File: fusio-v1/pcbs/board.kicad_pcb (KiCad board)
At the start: 2 copper layers, 210.5 x 76.5 mm, 72 parts

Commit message: add jlc silkscreen
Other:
- board text added: "JLCJLCJLCJLC"
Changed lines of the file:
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@@
 		(layer "Edge.Cuts")
+	)
+	(gr_text "JLCJLCJLCJLC"
+		(at 232.41 183.82 0)
+		(layer "B.SilkS")
+		(effects
+			(font
+				(size 1.5 1.5)
+				(thickness 0.3)
+				(bold yes)
+			)
+			(justify left bottom mirror)
+		)
 	)
 	(segment

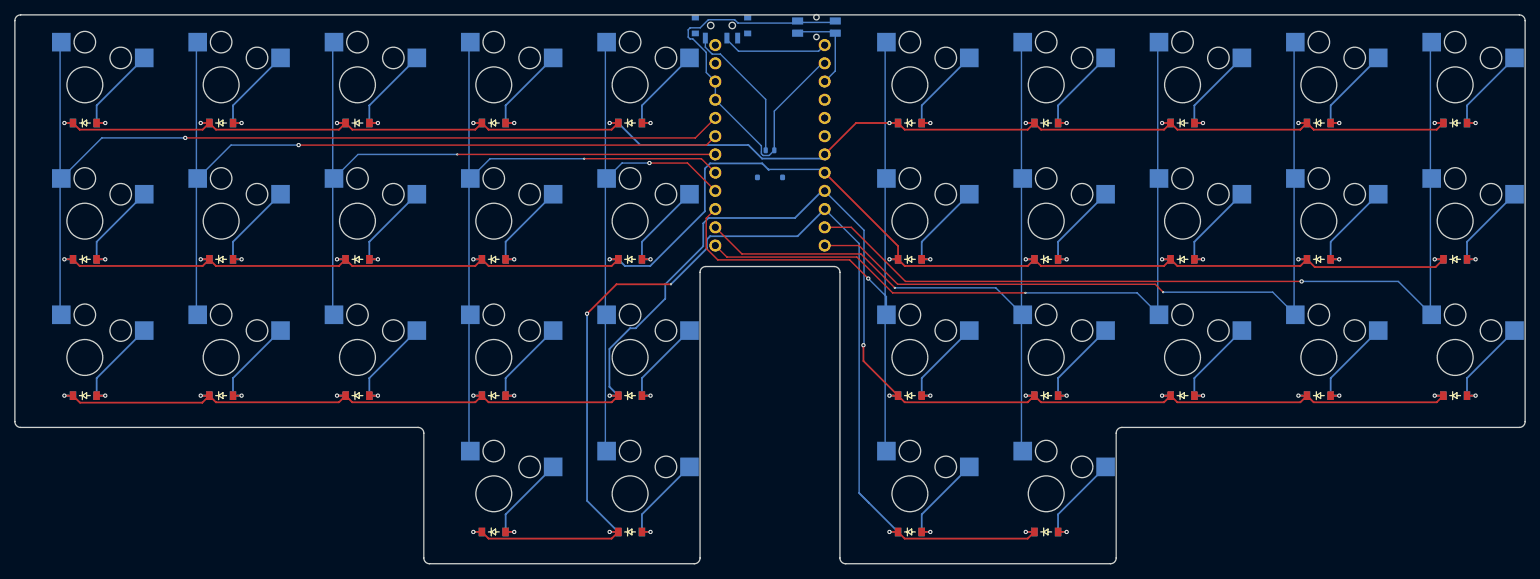
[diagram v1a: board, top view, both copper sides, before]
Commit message: support gateron
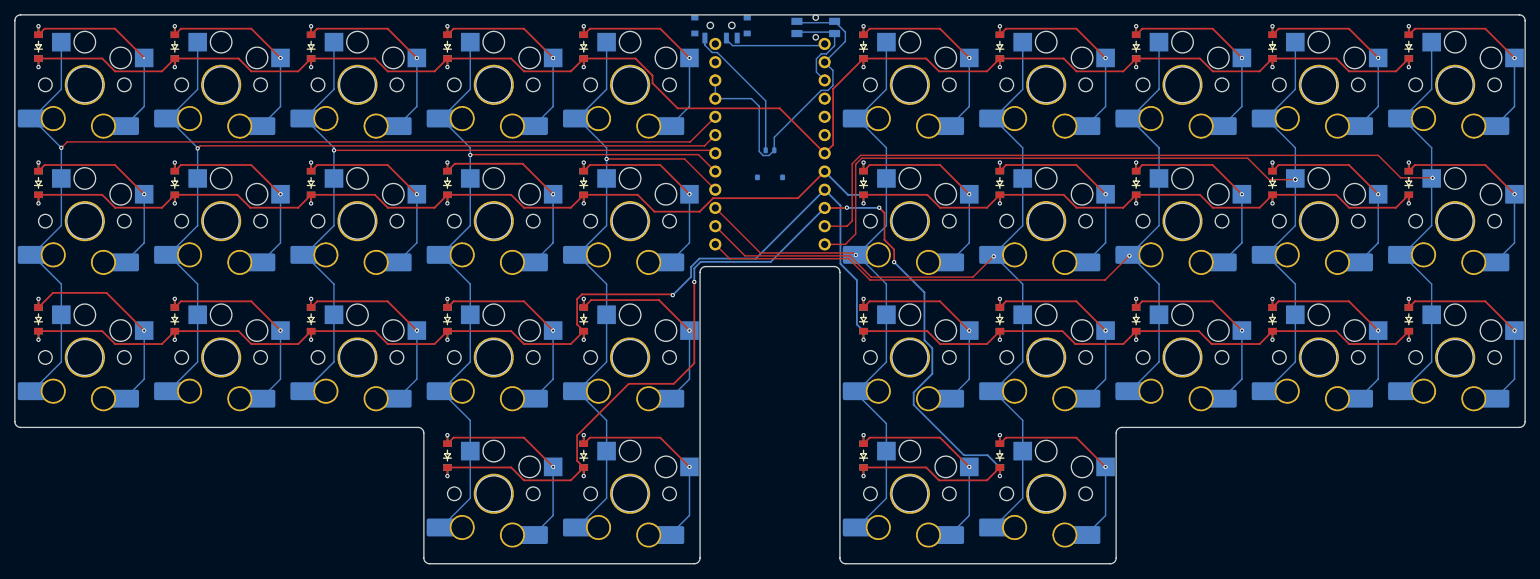
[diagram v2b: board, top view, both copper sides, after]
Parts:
- added S35: , ceoloide:switch_choc_v1_v2, B.Cu at (100.0, 156.0)
- added S36: , ceoloide:switch_choc_v1_v2, B.Cu at (100.0, 137.0)
- added S37: , ceoloide:switch_choc_v1_v2, B.Cu at (100.0, 118.0)
- added S38: , ceoloide:switch_choc_v1_v2, B.Cu at (119.0, 156.0)
- added S39: , ceoloide:switch_choc_v1_v2, B.Cu at (119.0, 137.0)
- added S40: , ceoloide:switch_choc_v1_v2, B.Cu at (119.0, 118.0)
- added S41: , ceoloide:switch_choc_v1_v2, B.Cu at (138.0, 156.0)
- added S42: , ceoloide:switch_choc_v1_v2, B.Cu at (138.0, 137.0)
- added S43: , ceoloide:switch_choc_v1_v2, B.Cu at (138.0, 118.0)
- added S44: , ceoloide:switch_choc_v1_v2, B.Cu at (157.0, 175.0)
- added S45: , ceoloide:switch_choc_v1_v2, B.Cu at (157.0, 156.0)
- added S46: , ceoloide:switch_choc_v1_v2, B.Cu at (157.0, 137.0)
- added S47: , ceoloide:switch_choc_v1_v2, B.Cu at (157.0, 118.0)
- added S48: , ceoloide:switch_choc_v1_v2, B.Cu at (176.0, 175.0)
- added S49: , ceoloide:switch_choc_v1_v2, B.Cu at (176.0, 156.0)
- added S50: , ceoloide:switch_choc_v1_v2, B.Cu at (176.0, 137.0)
- added S51: , ceoloide:switch_choc_v1_v2, B.Cu at (176.0, 118.0)
- added S52: , ceoloide:switch_choc_v1_v2, B.Cu at (215.0, 175.0)
- added S53: , ceoloide:switch_choc_v1_v2, B.Cu at (215.0, 156.0)
- added S54: , ceoloide:switch_choc_v1_v2, B.Cu at (215.0, 137.0)
- added S55: , ceoloide:switch_choc_v1_v2, B.Cu at (215.0, 118.0)
- added S56: , ceoloide:switch_choc_v1_v2, B.Cu at (234.0, 175.0)
- added S57: , ceoloide:switch_choc_v1_v2, B.Cu at (234.0, 156.0)
- added S58: , ceoloide:switch_choc_v1_v2, B.Cu at (234.0, 137.0)
- added S59: , ceoloide:switch_choc_v1_v2, B.Cu at (234.0, 118.0)
- added S60: , ceoloide:switch_choc_v1_v2, B.Cu at (253.0, 156.0)
- added S61: , ceoloide:switch_choc_v1_v2, B.Cu at (253.0, 137.0)
- added S62: , ceoloide:switch_choc_v1_v2, B.Cu at (253.0, 118.0)
- added S63: , ceoloide:switch_choc_v1_v2, B.Cu at (272.0, 156.0)
- added S64: , ceoloide:switch_choc_v1_v2, B.Cu at (272.0, 137.0)
- added S65: , ceoloide:switch_choc_v1_v2, B.Cu at (272.0, 118.0)
- added S66: , ceoloide:switch_choc_v1_v2, B.Cu at (291.0, 156.0)
- added S67: , ceoloide:switch_choc_v1_v2, B.Cu at (291.0, 137.0)
- added S68: , ceoloide:switch_choc_v1_v2, B.Cu at (291.0, 118.0)
- S1, S10, S11, S12, S13, S14, S15, S16, S17, S18, S19, S2, S20, S21, S22, S23, S24, S25, S26, S27, S28, S29, S3, S30, S31, S32, S33, S34, S4, S5, S6, S7, S8, S9: footprint ceoloide:switch_choc_v1_v2 -> ceoloide:switch_gateron_ks27_ks33
- moved D10 12.4 mm to (150.5, 169.7), turned to 90 degrees
- moved D11 12.4 mm to (150.5, 150.7), turned to 90 degrees
- moved D12 12.4 mm to (150.5, 131.7), turned to 90 degrees
- moved D13 12.4 mm to (150.5, 112.7), turned to 90 degrees
- moved D14 12.4 mm to (169.5, 169.7), turned to 90 degrees
- moved D15 12.4 mm to (169.5, 150.7), turned to 90 degrees
- moved D16 12.4 mm to (169.5, 131.7), turned to 90 degrees
- moved D17 12.4 mm to (169.5, 112.7), turned to 90 degrees
- moved D18 12.4 mm to (208.5, 169.7), turned to 90 degrees
- moved D19 12.4 mm to (208.5, 150.7), turned to 90 degrees
- moved D20 12.4 mm to (208.5, 131.7), turned to 90 degrees
- moved D21 12.4 mm to (208.5, 112.7), turned to 90 degrees
- moved D22 12.4 mm to (227.5, 169.7), turned to 90 degrees
- moved D23 12.4 mm to (227.5, 150.7), turned to 90 degrees
- moved D24 12.4 mm to (227.5, 131.7), turned to 90 degrees
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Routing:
- net P10: track 108.6 -> 134.8 mm, vias 1 -> 2
- net P16: track 128.5 -> 152.0 mm
- net P6: track 74.8 -> 96.4 mm
- net P5: track 93.2 -> 114.6 mm
- net P19: track 225.2 -> 243.0 mm
- net P8: track 105.0 -> 122.6 mm
- net P2: track 132.8 -> 150.0 mm
- net P3: track 112.8 -> 130.0 mm
- net P4: track 93.3 -> 110.4 mm
- net leftpinky_bottom: track 14.2 -> 30.8 mm, vias 1 -> 2
- net leftinner_bottom: track 14.2 -> 30.0 mm, vias 1 -> 2
- net leftindex_home: track 14.2 -> 30.0 mm, vias 1 -> 2
- net rightinner_top: track 14.2 -> 29.8 mm, vias 1 -> 2
- net rightindex_top: track 14.2 -> 29.8 mm, vias 1 -> 2
- net leftmiddle_top: track 14.2 -> 29.8 mm, vias 1 -> 2
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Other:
- board text removed: "JLCJLCJLCJLC"

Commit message: add jlc
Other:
- board text added: "JLCJLCJLCJLC"
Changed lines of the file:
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@@
 		(layer "Edge.Cuts")
+	)
+	(gr_text "JLCJLCJLCJLC"
+		(at 203.45 143.2 0)
+		(layer "B.SilkS")
+		(effects
+			(font
+				(size 1.5 1.5)
+				(thickness 0.3)
+				(bold yes)
+			)
+			(justify left bottom mirror)
+		)
 	)
 	(segment
